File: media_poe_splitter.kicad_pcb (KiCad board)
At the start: 4 copper layers, 70.7 x 66.1 mm, 76 parts, among them IC1 LAN7850-I_8JX, IC2 17791063215, IC3 93AA66C-I/SN, J1 Screw_Terminal_01x02, X1 7499811120, X2 68710614522, Y1 830055299

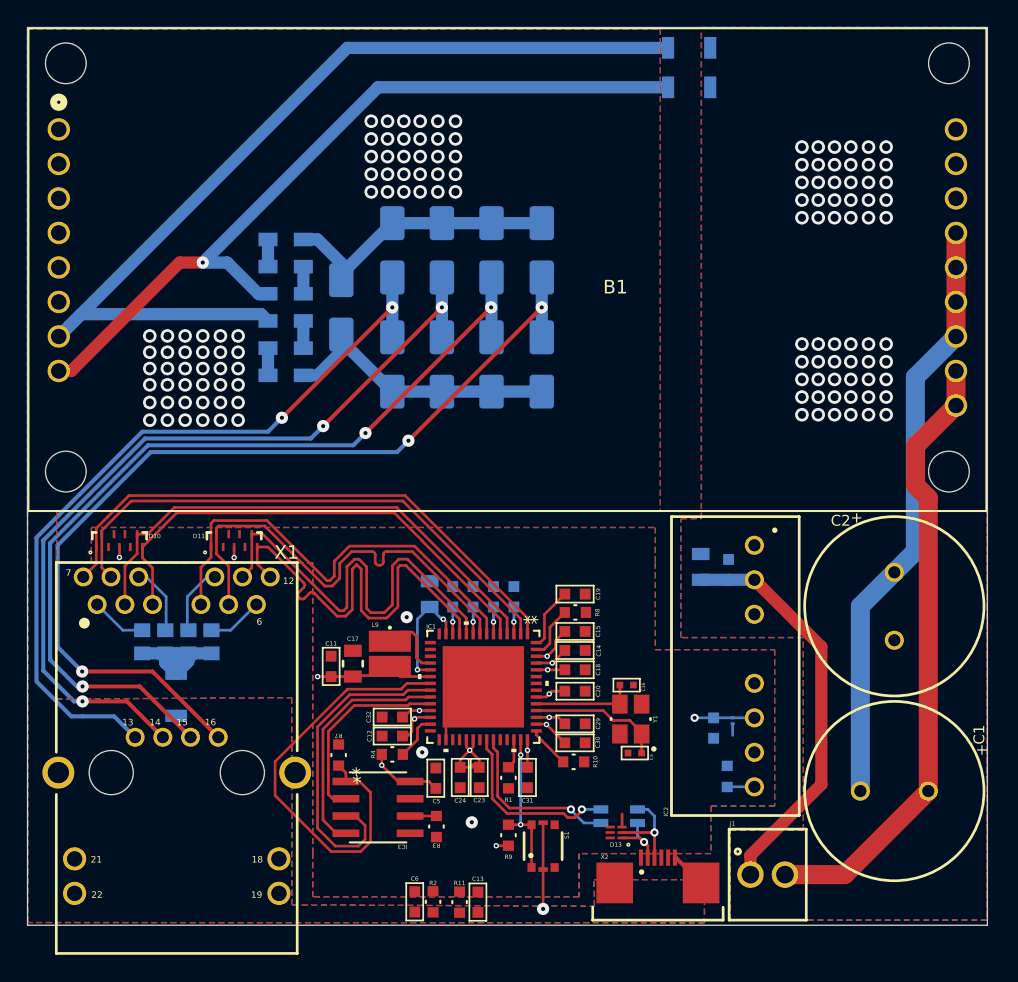
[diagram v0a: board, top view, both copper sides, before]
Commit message: Add MOSFET to 24V output for enable/disable capability
Signed-off-by: Marc 'risson' Schmitt <marc.schmitt@risson.space>
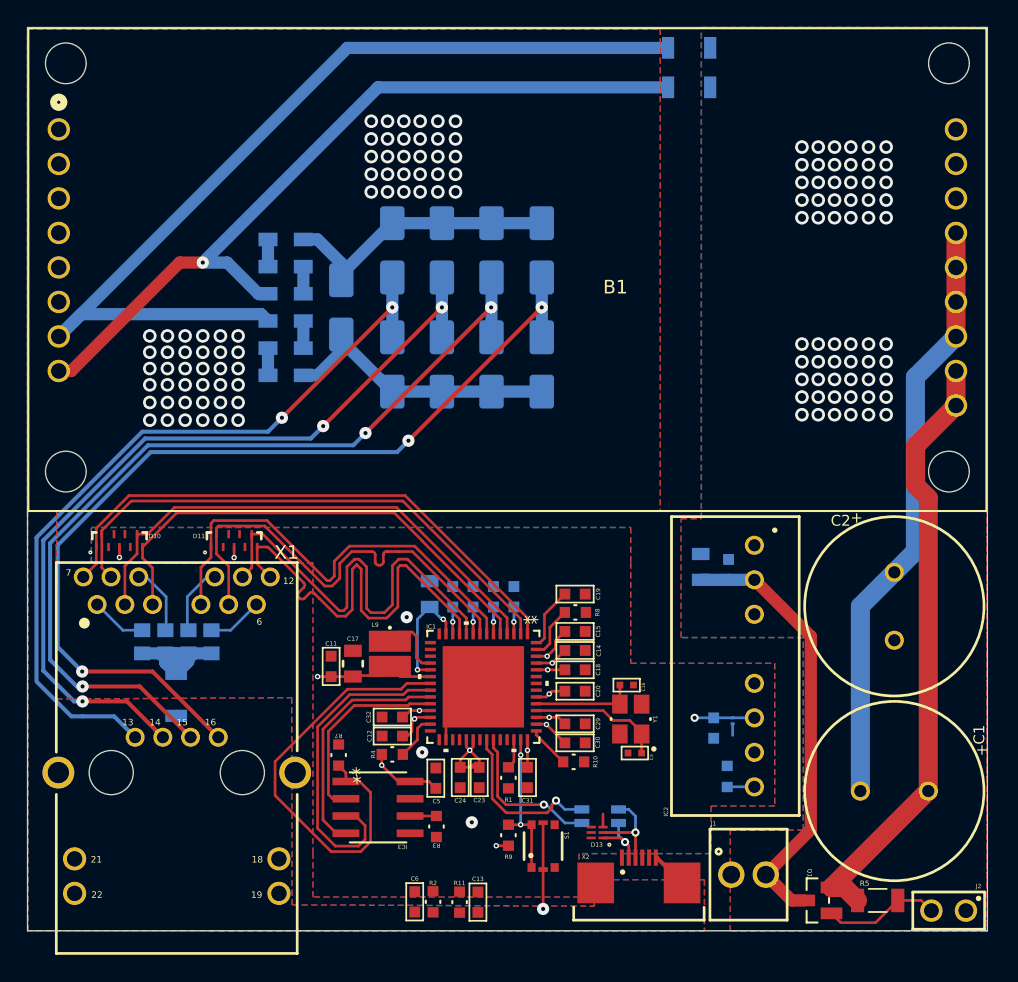
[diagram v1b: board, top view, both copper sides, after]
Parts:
- added J2: ~, 61300211121:61300211121, F.Cu at (87.8, 85.0)
- added Q1: DMP3099L-7, DMP3099L-7:DMP3099L-7, F.Cu at (78.2, 84.2)
- added R5: 100K, RC1206FR-07100KL:RC1206FR-07100KL, F.Cu at (82.6, 84.2)
- moved J1 1.41 mm to (73.1, 82.3)
- moved X2 1.40 mm to (65.0, 83.5)
- moved D13 1.40 mm to (61.9, 79.2)
- moved L7 1.40 mm to (62.1, 78.0)
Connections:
- B1 pad 10: Net-(B1-VOUT2-Pad10) -> Net-(Q1-S)
- B1 pad 9: Net-(B1-VOUT2-Pad10) -> Net-(Q1-S)
- C1 pad 1: Net-(B1-VOUT2-Pad10) -> Net-(Q1-S)
- C4 pad 1: Net-(IC2-+VIN) -> +24V
- C7 pad 1: Net-(IC2-+VIN) -> +24V
- IC2 pad 2: Net-(IC2-+VIN) -> +24V
- J1 pad 1: Net-(IC2-+VIN) -> GNDA
- J1 pad 2: Net-(B1-VOUT2-Pad10) -> +24V
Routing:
- net Net-(B1-VOUT2-Pad10): track 45.6 -> 0.00 mm
- net Net-(Q1-S): track 0.00 -> 44.9 mm
- net +24V: track 0.00 -> 32.4 mm
- net Net-(IC2-+VIN): track 29.9 -> 0.00 mm
- net Net-(Q1-G): track 0.00 -> 8.63 mm
- net /USBD_M: track 12.7 -> 11.3 mm
- net /USBD_P: track 13.4 -> 12.3 mm
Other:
- board size 70.7 x 66.1 mm -> 70.7 x 66.5 mm

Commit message: board: tweak track sizes and fill zones
Signed-off-by: Marc 'risson' Schmitt <marc.schmitt@risson.space>
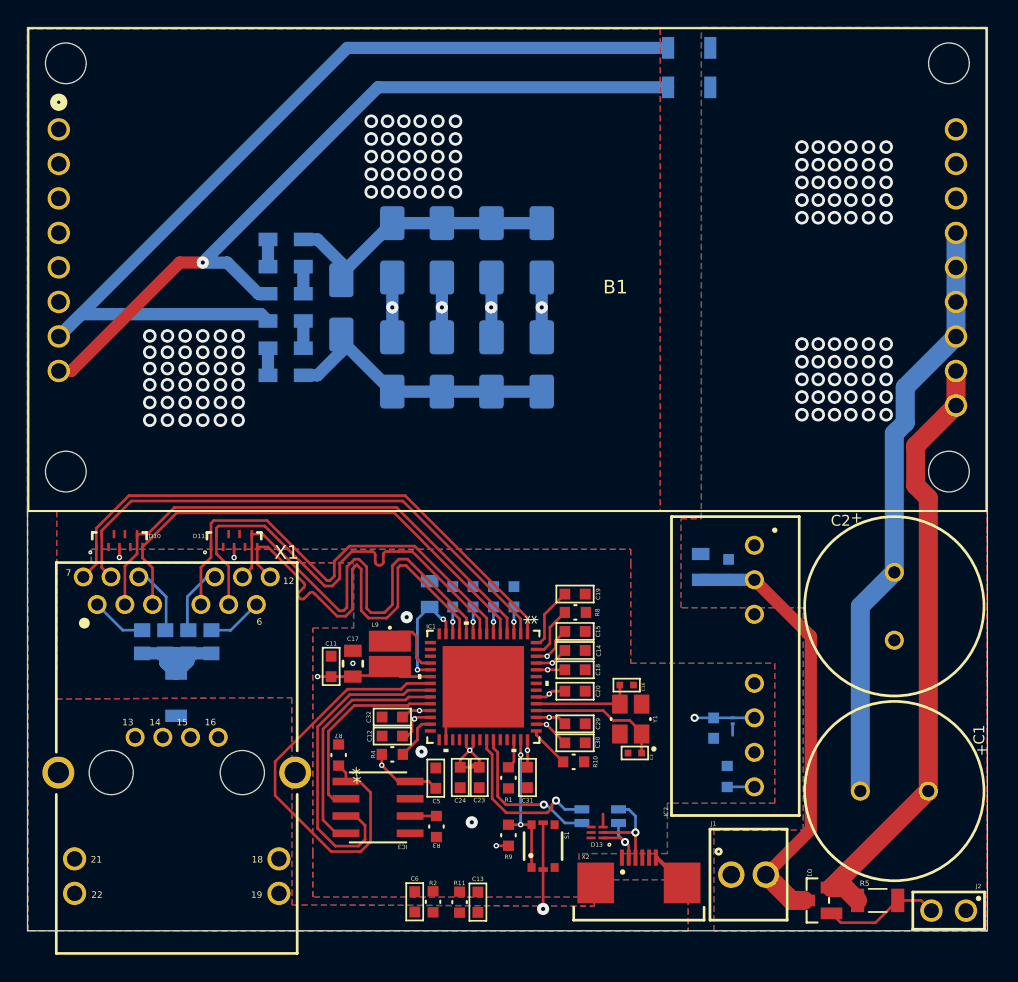
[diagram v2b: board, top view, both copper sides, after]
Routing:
- net /PAIR78: track 69.3 -> 45.9 mm, vias 3 -> 1
- net /PAIR45: track 65.4 -> 45.2 mm, vias 3 -> 1
- net /PAIR36: track 61.3 -> 57.5 mm, vias 3 -> 1
- net /PAIR12: track 57.1 -> 54.8 mm, vias 2 -> 1
- net GND: vias 5 -> 6
